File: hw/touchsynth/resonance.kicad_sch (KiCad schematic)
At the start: 27 parts, among them Q10 MMBT3904, Q11 BC847BS, U12 LM324, U2 TL072

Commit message: Schematic v2: hand-drawn sheet layouts with wires; MIDI in DNP
- draw.py/gen_sch2.py/layouts.py: placement + wiring per block, automatic
  labels for remaining split nets, short detection, junctions, KiCad
  endpoint-only connection semantics
- all 7 sheets laid out (ladder drawn as a transistor stack, diff amps,
  integrator with reset, R-2R DAC, ...); ERC 0 violations, netlist == design,
  145 simulated elements match
- MIDI input parts marked DNP (footprints kept)
- docs/touchsynth_schematic.pdf

Co-Authored-By: Claude Opus 5.5 (1M context) <noreply@anthropic.com>
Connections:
- net CVR_A: no longer names the net of C36.1, R58.2, R59.1
- net CVR_B: no longer names the net of C37.1, R59.2, R60.1
- net RESOUT: no longer names the net of C40.1, R70.2, TP17.1, U2.7
- net RES_DM: no longer names the net of R69.2, R70.1, U2.6 (-)
- net RES_DP: no longer names the net of R71.2, R72.1, U2.5 (+)
- net RES_FB: no longer names the net of C40.2, R73.1
- net RES_IN1: no longer names the net of Q11.2 (B1), R64.2, R65.1
- net RES_IN2: no longer names the net of Q11.5 (B2), R66.1
- net RES_RI: no longer names the net of C39.2, R64.1
- net VIR_B: no longer names the net of Q10.1 (B), R62.2
- net VIR_E: no longer names the net of Q10.2 (E), R63.1, U12.13 (-)
- net VIR_OUT: no longer names the net of R62.1, U12.14
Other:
- note added: "CV_RES: PWM filter and V-to-I converter (tail current of the resonance VCA)"
- note added: "Resonance VCA: differential pair, difference amplifier, AC-coupled feedback into the ladder (BIN2)"
- note removed: "CV_RES filter and V-to-I converter"
- note removed: "Resonance VCA and difference amplifier"
- note removed: "Test points"

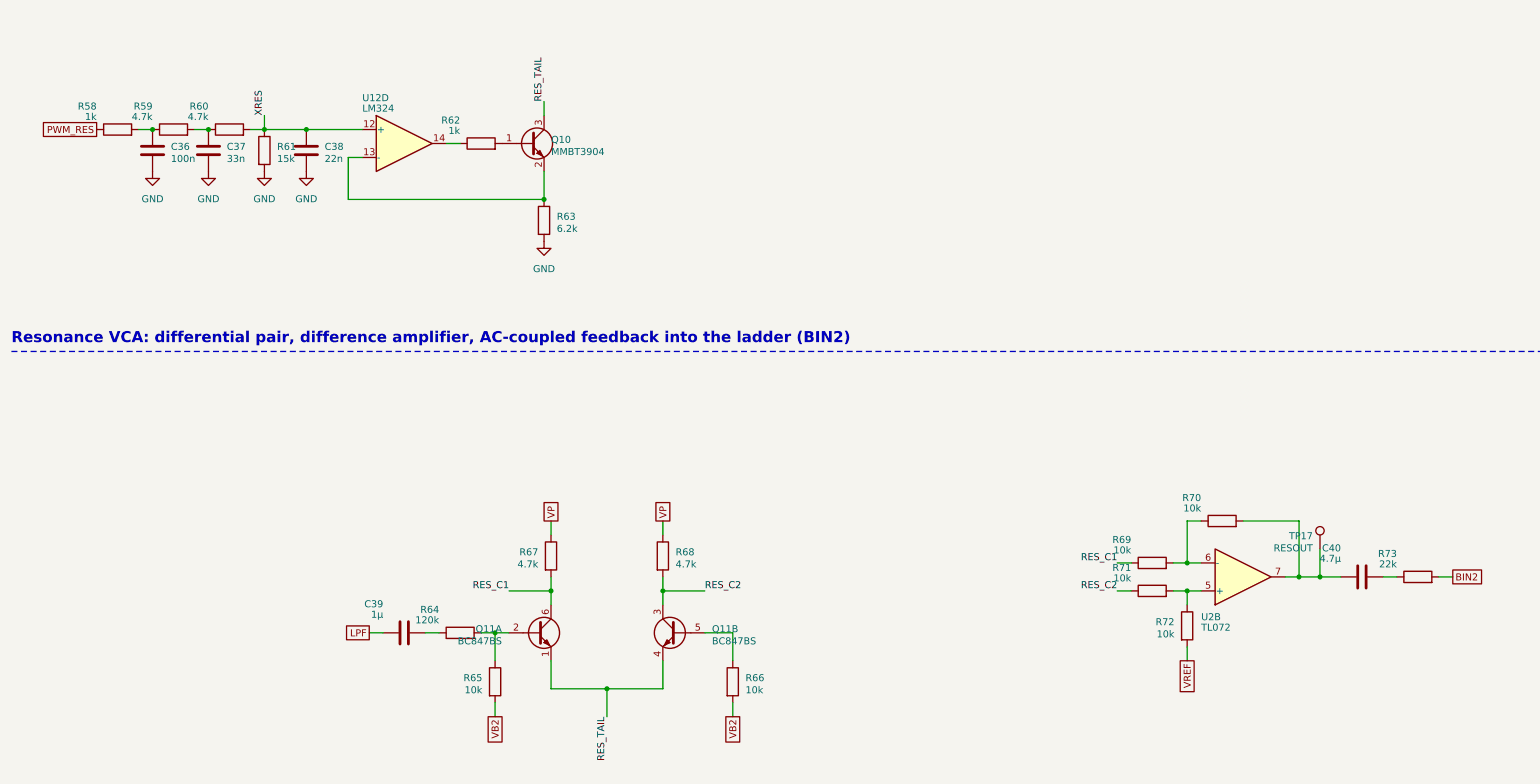
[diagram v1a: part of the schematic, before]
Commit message: PCB placement by functional block, silkscreen art, discrete LED resistors
- gen_pcb.py / pcb_place.py: 100 x 100 mm 2-layer board; keys, LEDs, connectors and test points fixed,
  ICs anchored per block, remaining parts placed greedily by connectivity inside their block
- blocks tile the circuit area with a 0.35 mm street for the dashed silkscreen frames and a reserved
  title tab each (pcb_art.py); piano keybed with hatched black keys; logo, resonant saw and ladder
  response curves on the front; signal-flow diagram on the back
- LED resistor arrays replaced by 16 discrete 4.7k 0603 (basic part) next to each LED
- deterministic schematic UUIDs, net name labels for PCB parity, op-amp re-pairing, fab.py

Co-Authored-By: Claude Opus 5.5 (1M context) <noreply@anthropic.com>
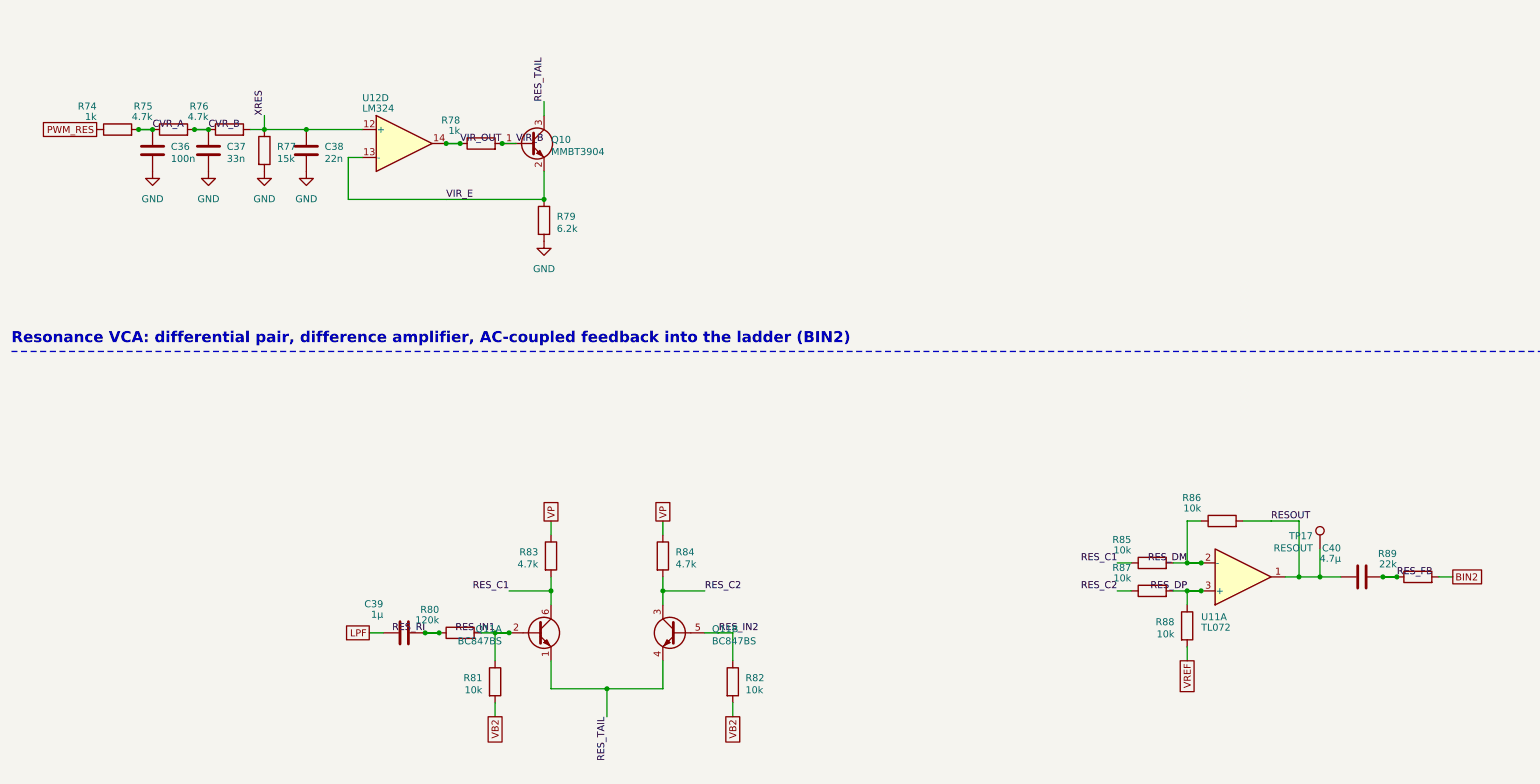
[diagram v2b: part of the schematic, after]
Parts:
- removed R58, R62: 1k, Resistor_SMD:R_0603_1608Metric, symbol Device:R
- removed R59, R60, R67, R68: 4.7k, Resistor_SMD:R_0603_1608Metric, symbol Device:R
- removed R61: 15k, Resistor_SMD:R_0603_1608Metric, symbol Device:R
- removed R63: 6.2k, Resistor_SMD:R_0603_1608Metric, symbol Device:R
- removed R64: 120k, Resistor_SMD:R_0603_1608Metric, symbol Device:R
- removed R65, R66, R69, R70, R71, R72: 10k, Resistor_SMD:R_0603_1608Metric, symbol Device:R
- removed R73: 22k, Resistor_SMD:R_0603_1608Metric, symbol Device:R
- removed U2: TL072, Package_SO:SOIC-8_3.9x4.9mm_P1.27mm, symbol Amplifier_Operational:TL072
- added R74, R78: 1k, Resistor_SMD:R_0603_1608Metric, symbol Device:R
- added R75, R76, R83, R84: 4.7k, Resistor_SMD:R_0603_1608Metric, symbol Device:R
- added R77: 15k, Resistor_SMD:R_0603_1608Metric, symbol Device:R
- added R79: 6.2k, Resistor_SMD:R_0603_1608Metric, symbol Device:R
- added R80: 120k, Resistor_SMD:R_0603_1608Metric, symbol Device:R
- added R81, R82, R85, R86, R87, R88: 10k, Resistor_SMD:R_0603_1608Metric, symbol Device:R
- added R89: 22k, Resistor_SMD:R_0603_1608Metric, symbol Device:R
- added U11: TL072, Package_SO:SOIC-8_3.9x4.9mm_P1.27mm, symbol Amplifier_Operational:TL072
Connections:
- net BIN2: now also R89.2
- net GND: now also R77.2, R79.2
- net PWM_RES: now also R74.1
- net RES_C1: now also R83.2, R85.1
- net RES_C2: now also R84.2, R87.1
- net VB2: now also R81.2, R82.2
- net VP: now also R83.1, R84.1
- net VREF: now also R88.2
- net XRES: now also R76.2, R77.1
- net RESOUT: now reaches C40.1, TP17.1
- net RESOUT: now also R86.2, U11.1
- net RES_IN1: now reaches Q11.2 (B1)
- net RES_IN1: now also R80.2, R81.1
- net RES_RI: now reaches C39.2
- net RES_RI: now also R80.1
- net VIR_B: now reaches Q10.1 (B)
- net VIR_B: now also R78.2
- net VIR_E: now reaches Q10.2 (E), U12.13 (-)
- net VIR_E: now also R79.1
- net RES_FB: now reaches C40.2
- net RES_FB: now also R89.1
- net CVR_A: now reaches C36.1
- net CVR_A: now also R74.2, R75.1
- net CVR_B: now reaches C37.1
- net CVR_B: now also R75.2, R76.1
- net VIR_OUT: now reaches U12.14
- net VIR_OUT: now also R78.1
- net RES_IN2: now reaches Q11.5 (B2)
- net RES_IN2: now also R82.1
- new net RES_DM: R85.2, R86.1, U11.2 (-)
- new net RES_DP: R87.2, R88.1, U11.3 (+)

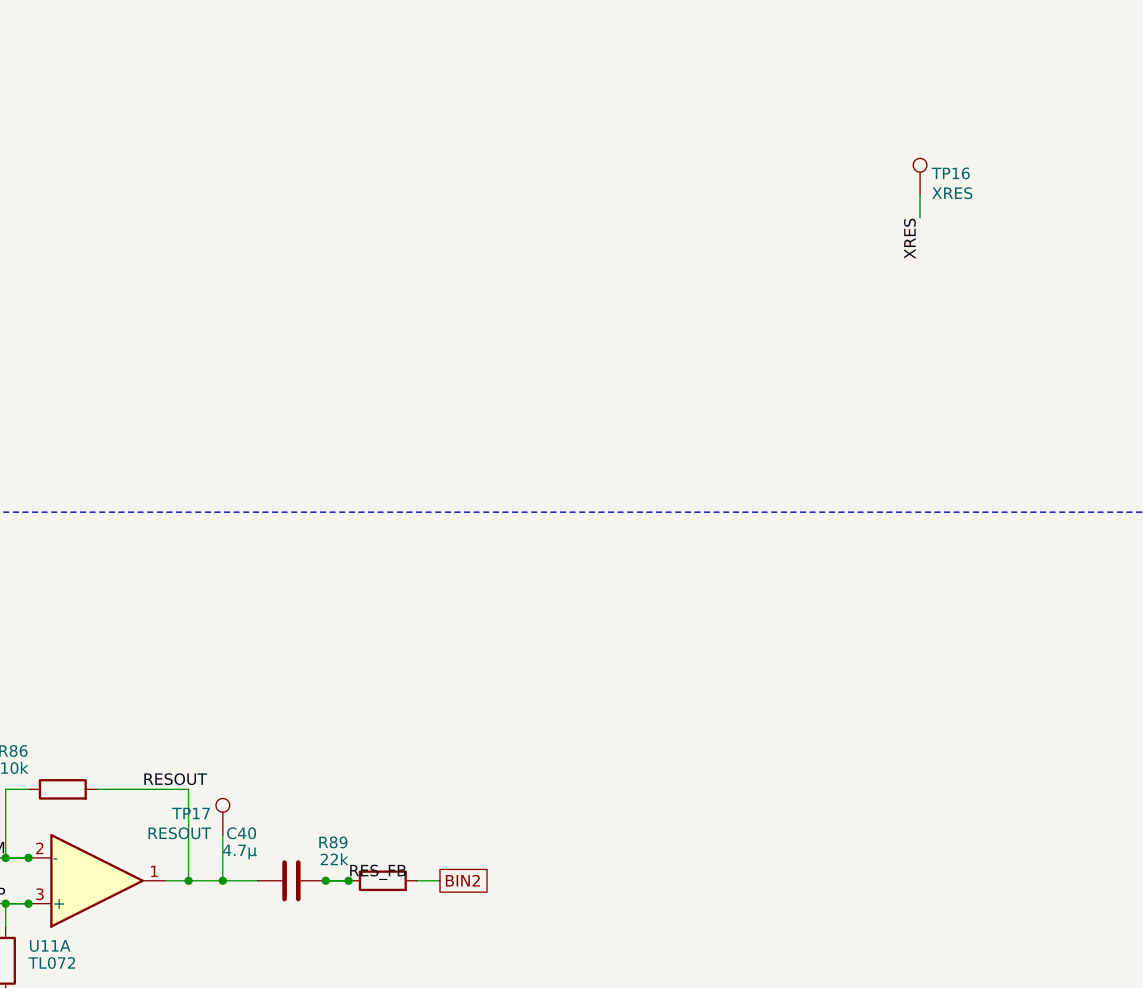
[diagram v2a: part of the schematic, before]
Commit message: 4-layer PCB: keys I/O row, trim DAC by the VCA, full routing and fab outputs
- 4 layers: F.Cu signals, In1 solid GND, In2 split power (VP analog / +5V digital / GND under the keys),
  B.Cu signals; no plane and no foreign tracks under the touch pads
- floorplan: analog blocks 72 x 36 mm in signal-flow order, right column MIDI / trim DAC / MCU,
  keys I/O row (touch muxes, LED shift registers) directly above the keys; shorter white keys,
  function pads flush with the keybed; test points inside their blocks, two THT scope-ground pins
- routing pipeline: plane stitch vias, pre-routed plane nets, Freerouting, GND via grid, island
  check, A* maze router for leftovers (pcb_maze.py), rip-up repair mode
- DRC: 0 violations, 0 unconnected, schematic parity OK; JLCPCB gerbers / BOM / CPL via fab.py
- silkscreen: back-side credits (design: cpldcpu & Claude Opus 5.5), vias kept out of the art

Co-Authored-By: Claude Opus 5.5 (1M context) <noreply@anthropic.com>
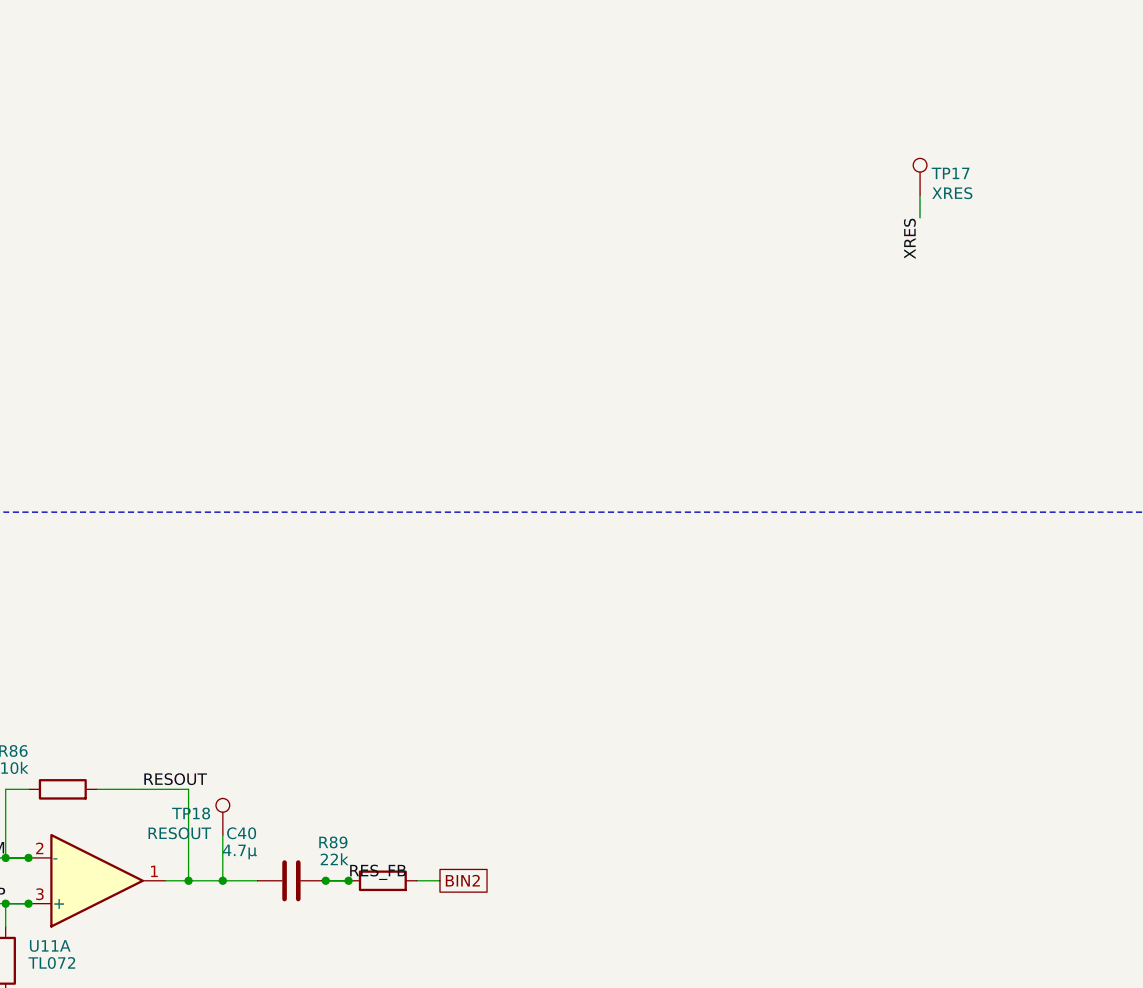
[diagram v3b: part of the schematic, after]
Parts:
- removed TP16: XRES, TestPoint:TestPoint_Pad_D1.0mm, symbol Connector:TestPoint
- added TP18: RESOUT, TestPoint:TestPoint_Pad_D1.0mm, symbol Connector:TestPoint
- TP17: value RESOUT -> XRES
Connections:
- net RESOUT: now also TP18.1; no longer TP17.1
- net XRES: now also TP17.1
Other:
- moved on the sheet: TP17
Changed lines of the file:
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@@
 		(on_board yes)
 		(dnp no)
-		(property "Reference" "TP17"
+		(property "Reference" "TP18"
 			(at 251.43 129.729 0)
 			(effects
@@
 			(project "touchsynth"
 				(path "/c42cd0d4-93b1-5178-97ee-fdd3025be2c6/c508aaa6-80f8-5132-b5bc-e1743a61f494"
-					(reference "TP17")
+					(reference "TP18")
 					(unit 1)
 				)
@@
 		(on_board yes)
 		(dnp no)
-		(property "Reference" "TP16"
+		(property "Reference" "TP17"
 			(at 331.5 58.609 0)
 			(effects
@@
 			(project "touchsynth"
 				(path "/c42cd0d4-93b1-5178-97ee-fdd3025be2c6/c508aaa6-80f8-5132-b5bc-e1743a61f494"
-					(reference "TP16")
+					(reference "TP17")
 					(unit 1)
 				)
